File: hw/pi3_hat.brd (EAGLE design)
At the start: 56.5 x 28.5 mm, 36 parts, among them U1 MAX13431E, U2 RT829910L_DFN, U3 STM32F051X6UFQFPN32, U4 DMMT5401, U5 DMG2305UX, X1 8.0MHz

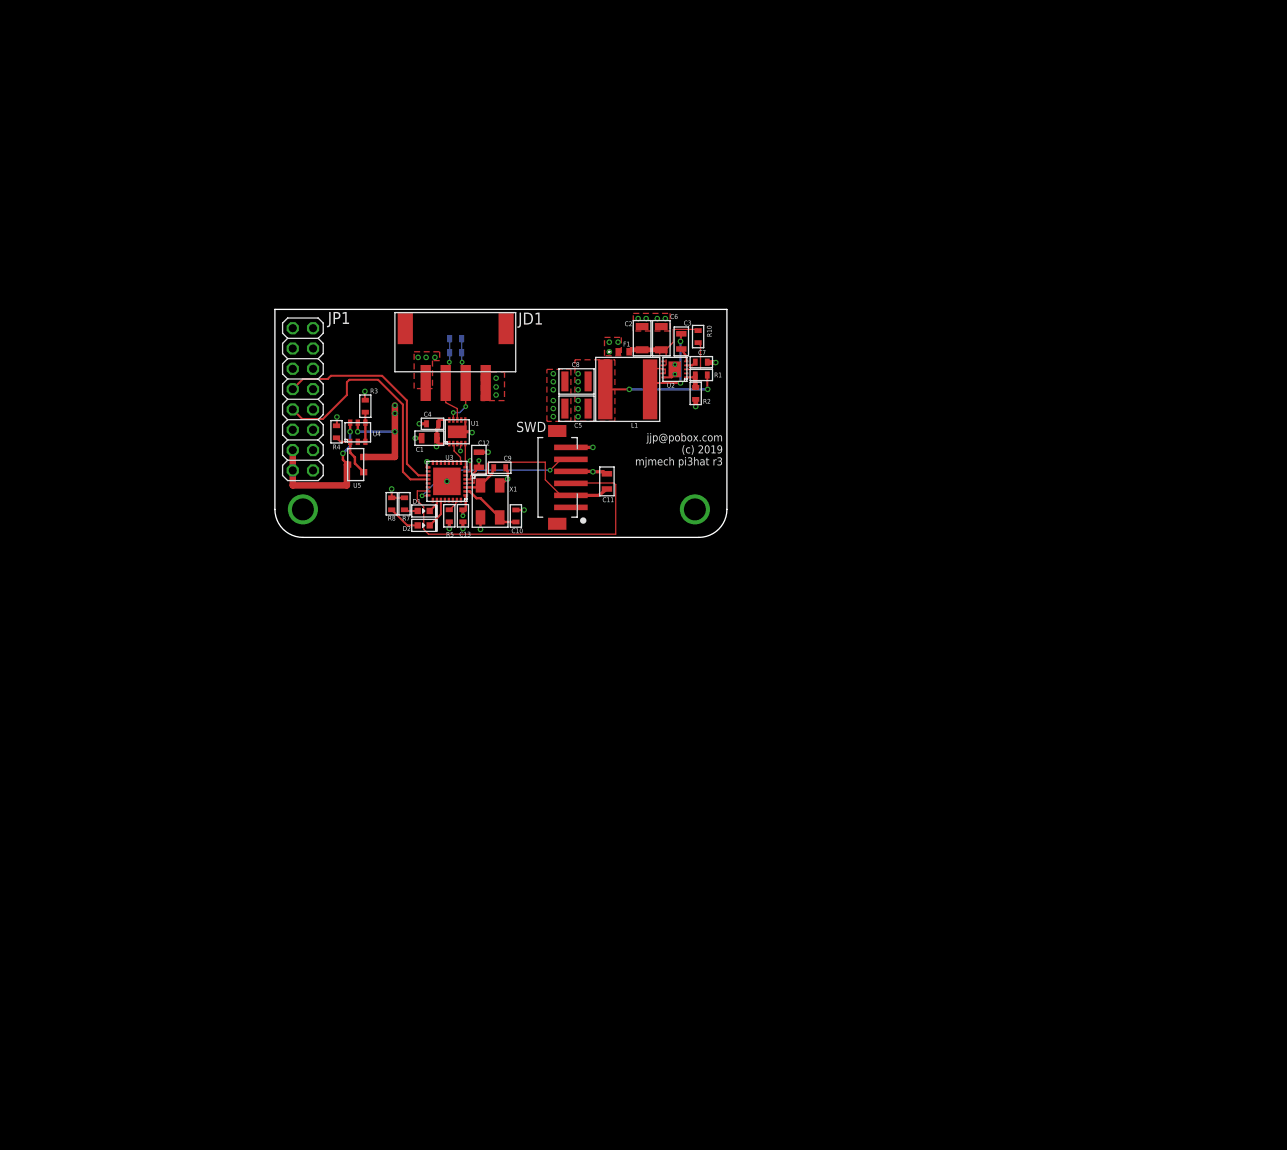
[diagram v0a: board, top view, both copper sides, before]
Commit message: Beginnings of r4 with multiple FD-CAN busses
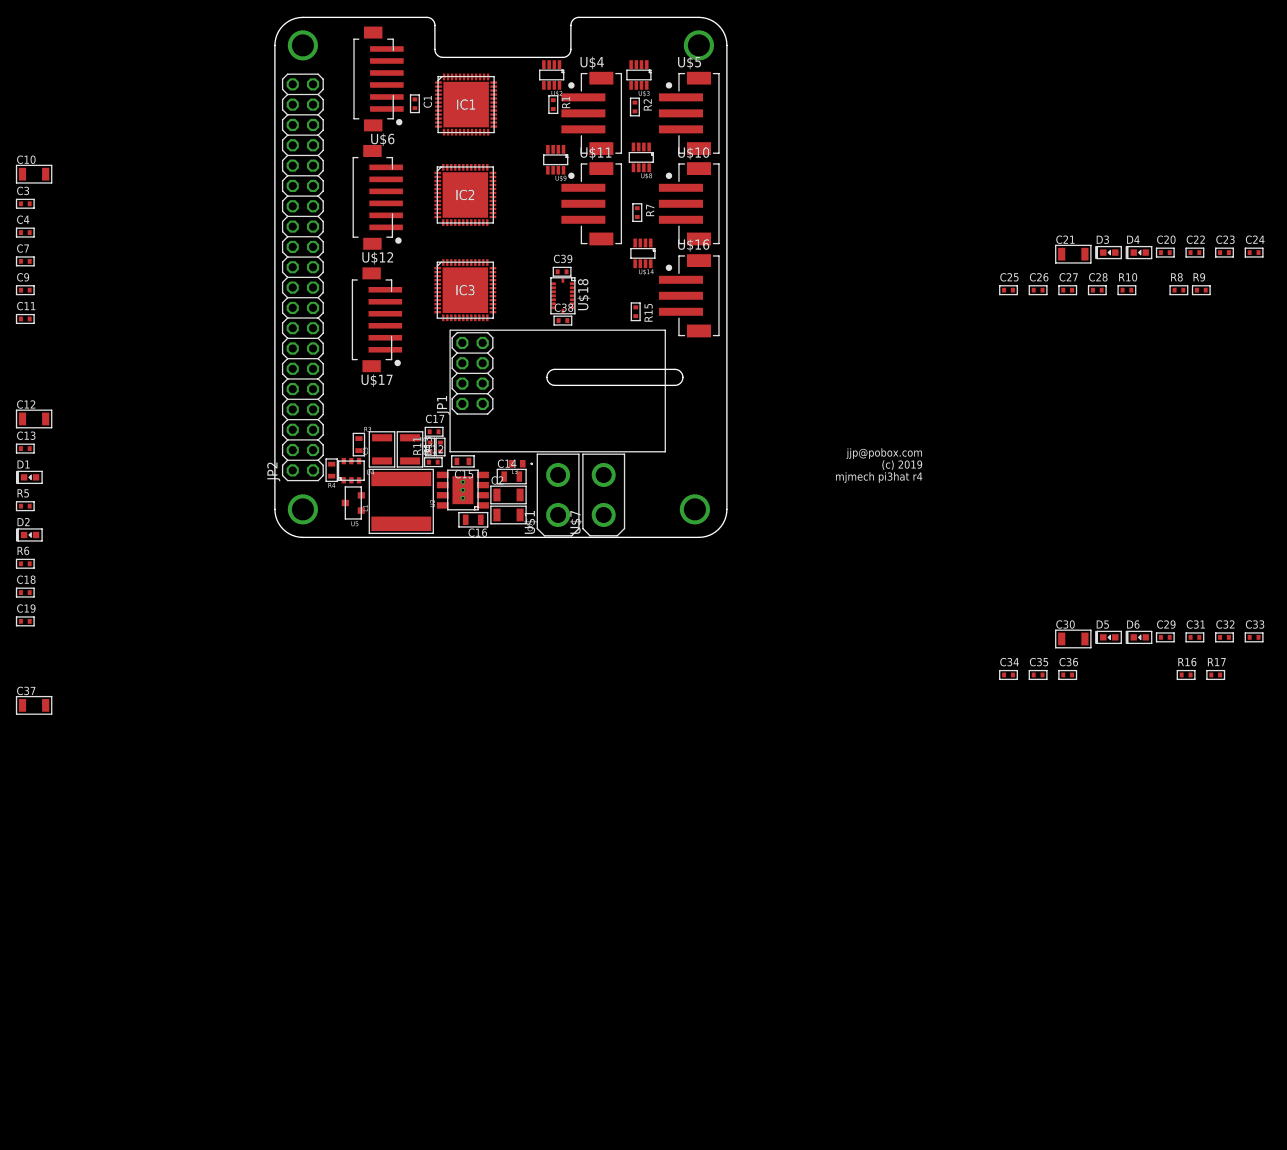
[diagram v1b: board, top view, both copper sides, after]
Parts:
- removed JD1: JST-XH4SMT_RA, odroid_shield:JST_XH_SMT_RA_4
- removed SWD: JST-ZH6SMT_VERT, controller:JST_B6B-ZR-SM4-TF(LF)(SN)
- removed U1: MAX13431E, controller:TDFN10
- removed U3: STM32F051X6UFQFPN32, pi3_hat:UFQFPN32
- removed X1: 8.0MHz, controller:ABM3B
- added C14, C16: .1uF 50V, mfpassives:C0805
- added C15: 0.01uF, mfpassives:C0603
- added C17: 3.3nF, mfpassives:C0402
- added C18, C19, C20, C22, C23, C24, C25, C27, C28, C29, C31, C32, C33, C34, C36, C38, C39: 0.1uF, mfpassives:C0402
- added C21, C30, C37: 10uF, mfpassives:C1206
- added C26, C35: 1uF, mfpassives:C0402
- added D3, D4, D5, D6: MF-LED-0603-RED, mfleds:LED0603
- added IC1, IC2, IC3: STM32G474CEU6, pi3_hat:QFN50P700X700X60-49N
- added JP2: (no value), pinhead:2X20
- added R11: 14k, mfpassives:R0402
- added R12: 115k, mfpassives:R0402
- added R13: 22.1k, mfpassives:R0402
- added R15: 120, mfpassives:R0402
- added R16, R17: (no value), mfpassives:R0402
- added U$1, U$7: XT30P, pi3_hat:XT30P
- added U$10, U$11, U$16, U$4, U$5: JST-PH3SMT_VERT, pi3_hat:JST_B3B_PH-SM4-TB(LF)(SN)
- added U$12, U$17, U$6: JST-ZH6SMT_VERT, pi3_hat:JST_B6B-ZR-SM4-TF(LF)(SN)
- added U$14, U$2, U$3, U$8, U$9: TCAN334GSOT23, pi3_hat:SOT23-8
- added U$18: BMI088LGA16, pi3_hat:LGA16
- C1, C3: value .1uF 50V -> 0.1uF; device mfpassives:C0805 -> mfpassives:C0402
- C10: value 10pF -> 10uF; device mfpassives:C0603 -> mfpassives:C1206
- C11: value .1uF 50V -> 1uF; device mfpassives:C0805 -> mfpassives:C0402
- C12: value .1uF 50V -> 10uF; device mfpassives:C0805 -> mfpassives:C1206
- C13, C4, C7: value 1uF -> 0.1uF; device mfpassives:C0603 -> mfpassives:C0402
- C2, C6: value 10uF 35V -> 10uF 50V
- C9: value 10pF -> 0.1uF; device mfpassives:C0603 -> mfpassives:C0402
- D2: value MF-LED-0603-GREEN -> MF-LED-0603-RED
- JP1: device pinhead:2X08 -> pinhead:2X04
- R1: value 53.6k 1% -> 120; device mfpassives:R0603 -> mfpassives:R0402
- R10: value 53.6k 1% -> (none); device mfpassives:R0603 -> mfpassives:R0402
- R2: value 10k 1% -> 120; device mfpassives:R0603 -> mfpassives:R0402
- R5, R6, R9: value 220 -> (none); device mfpassives:R0603 -> mfpassives:R0402
- R7, R8: value 220 -> 120; device mfpassives:R0603 -> mfpassives:R0402
- U2: value RT829910L_DFN -> AP64351SO8EP; device pi3_hat:10L_DFN -> pi3_hat:SO-8EP
- moved R8 102.0 mm to (113.0, 30.9), turned to 0 degrees
- moved R9 93.4 mm to (115.8, 30.9), flipped to the top
- moved C7 85.4 mm to (-31.2, 34.5)
- moved C3 83.8 mm to (-31.2, 41.7), turned to 0 degrees
- moved C11 75.5 mm to (-31.2, 27.3), turned to 0 degrees
- moved C10 73.8 mm to (-30.1, 45.4), turned to 0 degrees
- moved C9 63.3 mm to (-31.2, 30.9)
- moved R6 59.9 mm to (-31.2, -3.30), flipped to the top
- moved C4 56.2 mm to (-31.2, 38.1), turned to 0 degrees
- moved C12 55.8 mm to (-30.1, 14.8), turned to 0 degrees
- moved C13 55.3 mm to (-31.2, 11.1), turned to 0 degrees
- moved R10 53.9 mm to (106.5, 30.9), turned to 0 degrees
- moved R5 53.0 mm to (-31.2, 3.90), turned to 0 degrees
- moved D1 49.4 mm to (-30.6, 7.50), turned to 0 degrees
- moved D2 49.2 mm to (-30.6, 0.30), turned to 0 degrees
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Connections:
- removed net +18V: F1.1, JD1.4
- removed net 485_DIR: U1.3, U1.4, U3.7
- removed net 485_RX: U1.2, U3.9
- removed net 485_TX: U1.5, U3.8
- removed net NRST: C11.P$1, SWD.2, U3.4
- removed net PI_RX_3V: JP1.10, U3.19
- removed net POSTFUSE: C2.P$1, C6.P$1, F1.2, R10.P$1, U2.6, U2.7
- removed net RS485_N: JD1.2, R6.P$1, R9.P$1, U1.9
- removed net RS485_P: JD1.3, R6.P$2, R9.P$2, U1.8
- removed net SW: C3.P$2, L1.1, U2.8, U2.9
- new net I2C1_SCL: JP2.5
- new net I2C1_SDA: JP2.3
- new net ID_SCL: JP2.28
- new net ID_SDA: JP2.27
- new net IMU_ACC_INT: IC3.30, U$18.16
- new net IMU_CS1: IC3.26, U$18.14
- new net IMU_CS2: IC3.25, U$18.5
- new net IMU_GYRO_INT: IC3.31, U$18.12
- new net IMU_MISO: IC3.28, U$18.10, U$18.15
- new net IMU_MOSI: IC3.29, U$18.9
- new net IMU_SCK: IC3.27, U$18.8
- new net N$10: C14.P$1, C2.P$1, C6.P$1, F1.2, U2.2, U2.3
- new net N$14: C16.P$1, U2.1
- new net N$19: C15.P$1, U2.4
- new net N$20: C16.P$2, L1.1, U2.8
- new net N$21: C17.P$1, R11.P$2
- new net N$22: R11.P$1, U2.6
- new net N$23: R7.P$1, U$10.1, U$8.7
- new net N$24: R12.P$2, R13.P$1, U2.5
- new net N$25: R7.P$2, U$10.2, U$8.6
- new net N$26: R8.P$1, U$11.1, U$9.7
- new net N$27: R8.P$2, U$11.2, U$9.6
- new net N$28: D1.ANODE, R5.P$2
- new net N$29: D1.CATHODE, IC1.3
- new net N$30: D2.ANODE, R6.P$2
- new net N$31: D2.CATHODE, IC1.4
- new net N$32: C20.P$1, IC2.7, U$12.2
- new net N$33: IC2.37, U$12.3
- new net N$34: IC2.38, U$12.5
- new net N$37: D4.ANODE, R10.P$2
- new net N$38: D4.CATHODE, IC2.4
- new net N$39: IC2.33, U$9.4
- new net N$40: IC2.34, U$9.1
- new net N$41: IC2.42, U$8.4
- new net N$42: IC2.43, U$8.1
- new net N$45: R15.P$1, U$14.7, U$16.1
- new net N$46: R15.P$2, U$14.6, U$16.2
- new net N$47: C29.P$1, IC3.7, U$17.2
- new net N$48: IC3.37, U$17.3
- new net N$49: IC3.38, U$17.5
- new net N$50: D5.ANODE, R16.P$2
- new net N$51: D5.CATHODE, IC3.3
- new net N$52: D6.ANODE, R17.P$2
- new net N$53: D6.CATHODE, IC3.4
- new net N$54: IC3.33, U$14.4
- new net N$55: IC3.34, U$14.1
- new net N$9: F1.1, U$1.2, U$7.2
- new net NRF_CE: IC3.39, JP1.6
- new net NRF_CS: IC3.43, JP1.5
- new net NRF_IRQ: IC3.44, JP1.1
- new net NRF_MISO: IC3.41, JP1.2
- new net NRF_MOSI: IC3.42, JP1.3
- new net NRF_SCK: IC3.40, JP1.4
- new net SPI0_CS0: IC3.12, JP2.24
- new net SPI0_CS1: JP2.26
- new net SPI0_MISO: IC3.14, JP2.21
- new net SPI0_MOSI: IC3.15, JP2.19
- new net SPI0_SCLK: IC3.13, JP2.23
- new net SPI1_CS0: IC1.12, JP2.12
- new net SPI1_CS1: IC2.12, JP2.11
- new net SPI1_CS2: JP2.36
- new net SPI1_MISO: IC1.14, IC2.14, JP2.35
- new net SPI1_MOSI: IC1.15, IC2.15, JP2.38
- new net SPI1_SCLK: IC1.13, IC2.13, JP2.40
- net +3V3: now also C10.P$1, C11.P$1, C18.P$1, C19.P$1, C21.P$1, C22.P$1, C23.P$1, C24.P$1, C25.P$1, C26.P$1, C27.P$1, C28.P$1, C3.P$1, C30.P$1, C31.P$1, C32.P$1, C33.P$1, C34.P$1, C35.P$1, C36.P$1, C37.P$1, C38.P$1, C39.P$1, C7.P$1, C9.P$1, IC1.20, IC1.21, IC1.24, IC1.36, IC1.48, IC2.20, IC2.21, IC2.24, IC2.36, IC2.48, IC3.20, IC3.21, IC3.24, IC3.36, IC3.48, JP1.7, JP2.1, JP2.17, R10.P$1, R16.P$1, R17.P$1, R5.P$1, R6.P$1, R9.P$1, U$12.6, U$14.3, U$17.6, U$18.11, U$18.3, U$2.3, U$3.3, U$6.6, U$8.3, U$9.3; no longer C1.P$1, JP1.1, R7.P$2, R8.P$2, SWD.6, U1.1, U1.10, U3.1, U3.17, U3.5
- net +5V: now also JP2.2, JP2.4; no longer JP1.2, JP1.4
- net GND: now also C14.P$2, C15.P$2, C17.P$2, C18.P$2, C19.P$2, C20.P$2, C21.P$2, C22.P$2, C23.P$2, C24.P$2, C25.P$2, C26.P$2, C27.P$2, C28.P$2, C29.P$2, C3.P$2, C30.P$2, C31.P$2, C32.P$2, C33.P$2, C34.P$2, C35.P$2, C36.P$2, C37.P$2, C38.P$2, C39.P$2, IC1.19, IC1.23, IC1.35, IC1.47, IC1.49, IC2.19, IC2.23, IC2.35, IC2.47, IC2.49, IC3.19, IC3.23, IC3.35, IC3.47, IC3.49, JP1.8, JP2.14, JP2.20, JP2.25, JP2.30, JP2.34, JP2.39, JP2.6, JP2.9, R13.P$2, U$1.1, U$10.3, U$11.3, U$12.4, U$14.2, U$14.5, U$14.8, U$16.3, U$17.4, U$18.4, U$18.6, U$18.7, U$2.2, U$2.5, U$2.8, U$3.2, U$3.5, U$3.8, U$4.3, U$5.3, U$6.4, U$7.1, U$8.2, U$8.5, U$8.8, U$9.2, U$9.5, U$9.8, U2.7, U2.P3, U2.PAD; no longer JD1.1, JP1.14, JP1.6, JP1.9, R2.P$2, R5.P$2, SWD.4, U1.6, U1.PAD, U2.10, U2.P0, U3.P, X1.2, X1.4
- net N$11: now also IC1.33, U$3.4; no longer R1.P$2, R2.P$1, U2.1
- net N$12: now also IC1.34, U$3.1; no longer SWD.5, U3.24
- net N$13: now also C1.P$1, IC1.7, U$6.2; no longer SWD.3, U3.23
- net N$15: now also IC1.37, U$6.3; no longer D1.ANODE, R7.P$1
- net N$16: now also IC1.38, U$6.5; no longer D2.ANODE, R8.P$1
- net N$17: now also IC1.42, U$2.4; no longer D1.CATHODE, U3.26
- net N$18: now also IC1.43, U$2.1; no longer D2.CATHODE, U3.27
- net N$2: now also R1.P$1, U$2.7, U$4.1; no longer C7.P$1, U2.4
- net N$35: now also D3.ANODE, R9.P$2; no longer C9.P$1, U3.3, X1.1
- net N$36: now also D3.CATHODE, IC2.3; no longer C10.P$1, U3.2, X1.3
- net N$4: now also R1.P$2, U$2.6, U$4.2; no longer R5.P$1, U3.31
- net N$7: now also R2.P$1, U$3.7, U$5.1; no longer R10.P$2, U2.3
- net N$8: now also R2.P$2, U$3.6, U$5.2; no longer C3.P$1, U2.5
- net PI_TX_3V: now also JP2.8; no longer JP1.8, U3.20
- net REGOUT: now also R12.P$1; no longer R1.P$1
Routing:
- net N$13: track 42.6 -> 0.00 mm
- net REGOUT: track 30.8 -> 0.00 mm, vias 12 -> 0
- net PI_TX_3V: track 30.5 -> 0.00 mm
- net PI_RX_3V: track 27.4 -> 0.00 mm
- net GND: track 25.2 -> 0.00 mm, vias 28 -> 0
- net NRST: track 23.2 -> 0.00 mm
- net N$12: track 21.3 -> 0.00 mm, vias 2 -> 0
- net +5V: track 19.7 -> 0.00 mm, vias 2 -> 0
- net +3V3: track 19.7 -> 0.00 mm, vias 6 -> 0
- net RS485_N: track 11.5 -> 0.00 mm, vias 3 -> 0
- net RS485_P: track 11.3 -> 0.00 mm, vias 1 -> 0
- net POSTFUSE: track 10.8 -> 0.00 mm
- net SW: track 10.3 -> 0.00 mm, vias 2 -> 0
- net N$36: track 7.86 -> 0.00 mm
- net N$5: track 6.53 -> 0.00 mm
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- removed copper zone on layer 1, net +18V
- removed copper zone on layer 15, net +18V
- removed copper zone on layer 15, net +3V3
- removed copper zone on layer 1, net GND
- removed copper zone on layer 2, net GND
- removed copper zone on layer 1, net POSTFUSE
- removed copper zone on layer 1, net REGOUT
- removed copper zone on layer 15, net REGOUT
- removed copper zone on layer 1, net SW
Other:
- board size 56.5 x 28.5 mm -> 56.5 x 65 mm
- board text added: "mjmech pi3hat r4"
- board text removed: "mjmech pi3hat r3"

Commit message: Fix up stm32 pinouts, add eeprom and test points
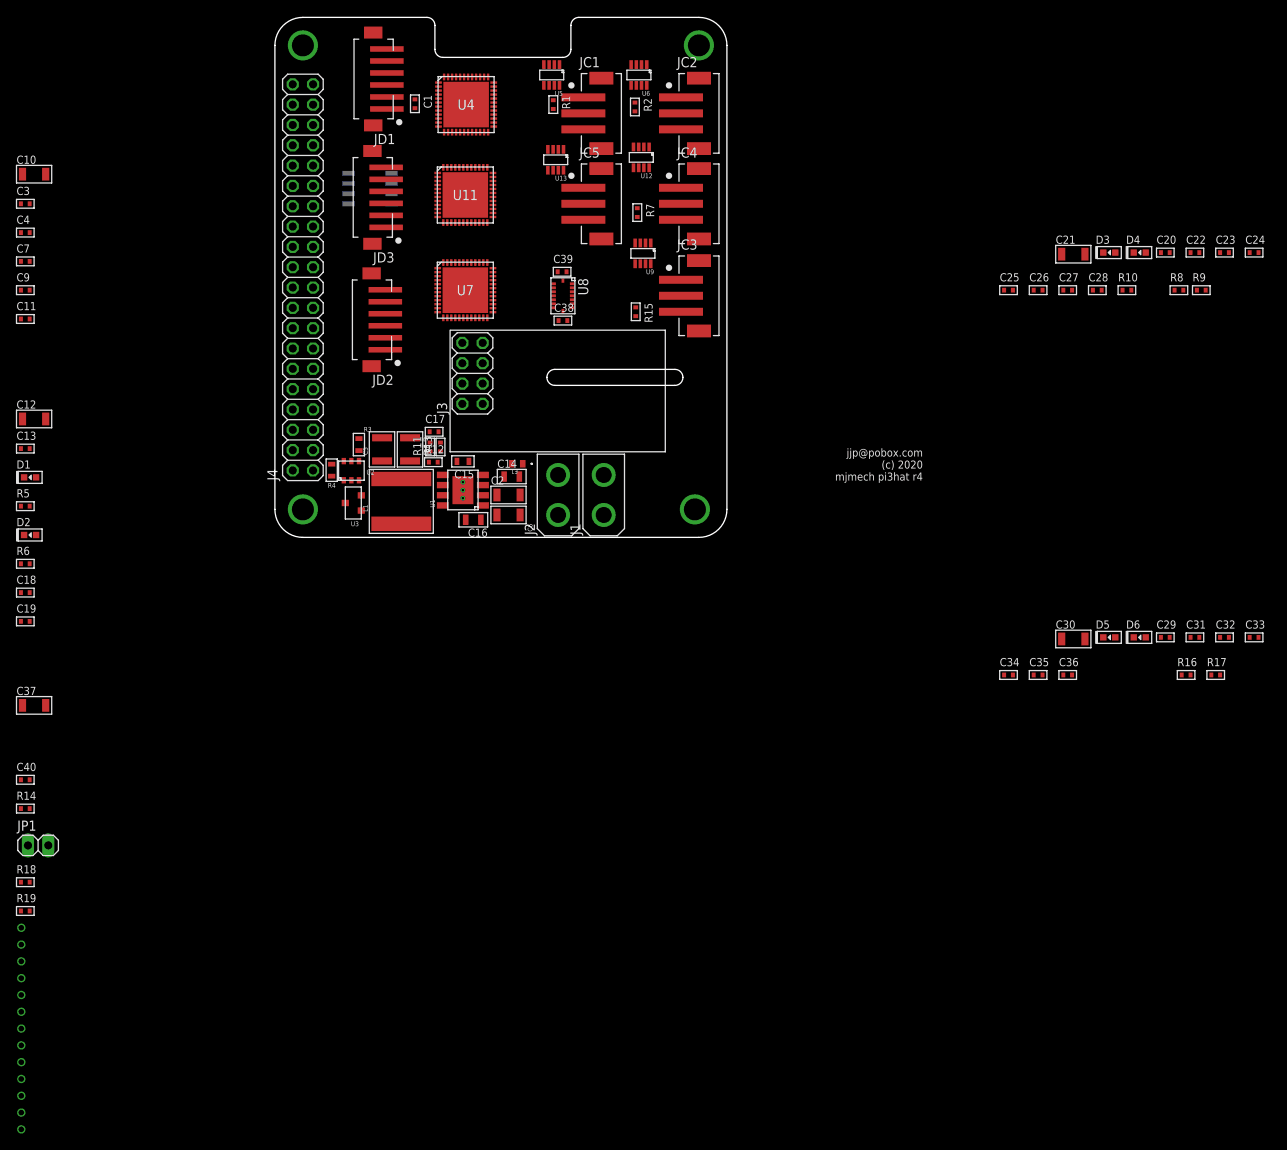
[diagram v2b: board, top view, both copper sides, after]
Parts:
- removed IC1: STM32G474CEU6, pi3_hat:QFN50P700X700X60-49N
- removed U$2: TCAN334GSOT23, pi3_hat:SOT23-8
- added +5V, GND, REGOUT, SPI0_CS0, SPI0_MISO, SPI0_MOSI, SPI0_SCLK, SPI1_CS0, SPI1_CS1, SPI1_MISO, SPI1_MOSI, SPI1_SCLK, V+: PAD24AWG_PAD, pi3_hat:24AWG_PAD
- added C40: 0.1uF, mfpassives:C0402
- added J3: (no value), pinhead:2X04
- added R14: 1k, mfpassives:R0402
- added R18, R19: 3.9k 1%, mfpassives:R0402
- added U1: AP64351SO8EP, pi3_hat:SO-8EP
- added U10: CAT24C32SOIC8, pi3_hat:SOIC8
- added U3: DMG2305UX, pi3_hat:SOT23
- JP1: device pinhead:2X04 -> pinhead:1X02
- U2: value AP64351SO8EP -> DMMT5401; device pi3_hat:SO-8EP -> pi3_hat:SOT26
- U4: value DMMT5401 -> STM32G474CEU6; device pi3_hat:SOT26 -> pi3_hat:QFN50P700X700X60-49N
- U5: value DMG2305UX -> TCAN334GSOT23; device pi3_hat:SOT23 -> pi3_hat:SOT23-8
- moved JP1 80.2 mm to (-29.6, -38.5), turned to 0 degrees
- moved U5 59.0 mm to (34.6, 57.8), turned to 180 degrees
- moved U4 48.0 mm to (23.9, 54.1)
- moved U2 14.2 mm to (9.56, 8.34), turned to 0 degrees
- renumbered IC2 to U11, IC3 to U7, JP2 to J4, U$1 to J2, U$10 to JC4, U$11 to JC5, U$12 to JD3, U$14 to U9, U$16 to JC3, U$17 to JD2, U$18 to U8, U$3 to U6, U$4 to JC1, U$5 to JC2, U$6 to JD1, U$7 to J1, U$8 to U12, U$9 to U13
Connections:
- removed net N$12: IC1.34, U6.1
- removed net N$9: F1.1, J1.2, J2.2
- new net N$100: U4.34, U6.1
- new net N$44: JP1.2, R14.P$2, U10.7
- new net V+: F1.1, J1.2, J2.2, V+.P$1
- net +3V3: now also C40.P$1, J3.7, R14.P$1, R18.P$1, R19.P$1, U10.8, U11.23, U11.35, U11.4, U4.1, U4.20, U4.21, U4.23, U4.35, U4.48, U5.3, U7.23, U7.3, U7.35; no longer IC1.20, IC1.21, IC1.24, IC1.36, IC1.48, JP1.7, U$2.3, U11.24, U11.36, U7.24, U7.36
- net +5V: now also +5V.P$1, U2.6, U3.3; no longer U4.6, U5.3
- net GND: now also C40.P$2, GND.P$1, J3.8, JP1.1, U1.7, U1.P1, U1.P2, U1.P3, U1.PAD, U10.1, U10.2, U10.3, U10.4, U11.3, U4.3, U4.4, U4.49, U5.2, U5.5, U5.8, U7.4; no longer IC1.19, IC1.23, IC1.35, IC1.47, IC1.49, JP1.8, U$2.2, U$2.5, U$2.8, U11.19, U11.23, U11.35, U11.47, U2.7, U2.P1, U2.P2, U2.P3, U2.PAD, U7.19, U7.23, U7.35, U7.47
- net ID_SCL: now also R19.P$2, U10.6
- net ID_SDA: now also R18.P$2, U10.5
- net IMU_CS1: now also U7.25; no longer U7.26
- net IMU_CS2: now also U7.24; no longer U7.25
- net IMU_MISO: now also U7.27; no longer U7.28
- net IMU_MOSI: now also U7.28; no longer U7.29
- net IMU_SCK: now also U7.26; no longer U7.27
- net N$1: now also U2.2, U2.3, U2.4; no longer U4.2, U4.3, U4.4
- net N$10: now also U1.2, U1.3; no longer U2.2, U2.3
- net N$11: now also U4.33; no longer IC1.33
- net N$13: now also U4.7; no longer IC1.7
- net N$14: now also U1.1; no longer U2.1
- net N$15: now also U4.36; no longer IC1.37
- net N$16: now also U4.37; no longer IC1.38
- net N$17: now also U4.41, U5.4; no longer IC1.42, U$2.4
- net N$18: now also U4.42, U5.1; no longer IC1.43, U$2.1
- net N$19: now also U1.4; no longer U2.4
- net N$2: now also U5.7; no longer U$2.7
- net N$20: now also U1.8; no longer U2.8
- net N$22: now also U1.6; no longer U2.6
- net N$24: now also U1.5; no longer U2.5
- net N$29: now also U4.5; no longer IC1.3
- net N$31: now also U4.6; no longer IC1.4
- net N$33: now also U11.36; no longer U11.37
- net N$34: now also U11.37; no longer U11.38
- net N$36: now also U11.5; no longer U11.3
- net N$38: now also U11.6; no longer U11.4
- net N$4: now also U5.6; no longer U$2.6
- net N$41: now also U11.41; no longer U11.42
- net N$42: now also U11.42; no longer U11.43
- net N$48: now also U7.36; no longer U7.37
- net N$49: now also U7.37; no longer U7.38
- net N$5: now also U2.1, U3.1; no longer U4.1, U5.1
- net N$51: now also U7.5; no longer U7.3
- net N$53: now also U7.6; no longer U7.4
- net NRF_CE: now also J3.6, U7.44; no longer JP1.6, U7.39
- net NRF_CS: now also J3.5, U7.38; no longer JP1.5, U7.43
- net NRF_IRQ: now also J3.1, U7.45; no longer JP1.1, U7.44
- net NRF_MISO: now also J3.2, U7.42; no longer JP1.2, U7.41
- net NRF_MOSI: now also J3.3, U7.43; no longer JP1.3, U7.42
- net NRF_SCK: now also J3.4, U7.41; no longer JP1.4, U7.40
- net REGOUT: now also REGOUT.P$1, U2.5, U3.2; no longer U4.5, U5.2
- net SPI0_CS0: now also SPI0_CS0.P$1
- net SPI0_MISO: now also SPI0_MISO.P$1
- net SPI0_MOSI: now also SPI0_MOSI.P$1
- net SPI0_SCLK: now also SPI0_SCLK.P$1
- net SPI1_CS0: now also SPI1_CS0.P$1, U4.12; no longer IC1.12
- net SPI1_CS1: now also SPI1_CS1.P$1
- net SPI1_MISO: now also SPI1_MISO.P$1, U4.14; no longer IC1.14
- net SPI1_MOSI: now also SPI1_MOSI.P$1, U4.15; no longer IC1.15
- net SPI1_SCLK: now also SPI1_SCLK.P$1, U4.13; no longer IC1.13
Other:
- board text added: "(c) 2020"
- board text removed: "(c) 2019"
